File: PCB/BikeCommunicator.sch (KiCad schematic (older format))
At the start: 14 parts, among them SW1 SW_SPST_LED, SW2 SW_SPST_LED, SW3 SW_SPST_LED, SW4 SW_SPST_LED, U1 HW-108_DC-DC, U2 HTCC-AB01

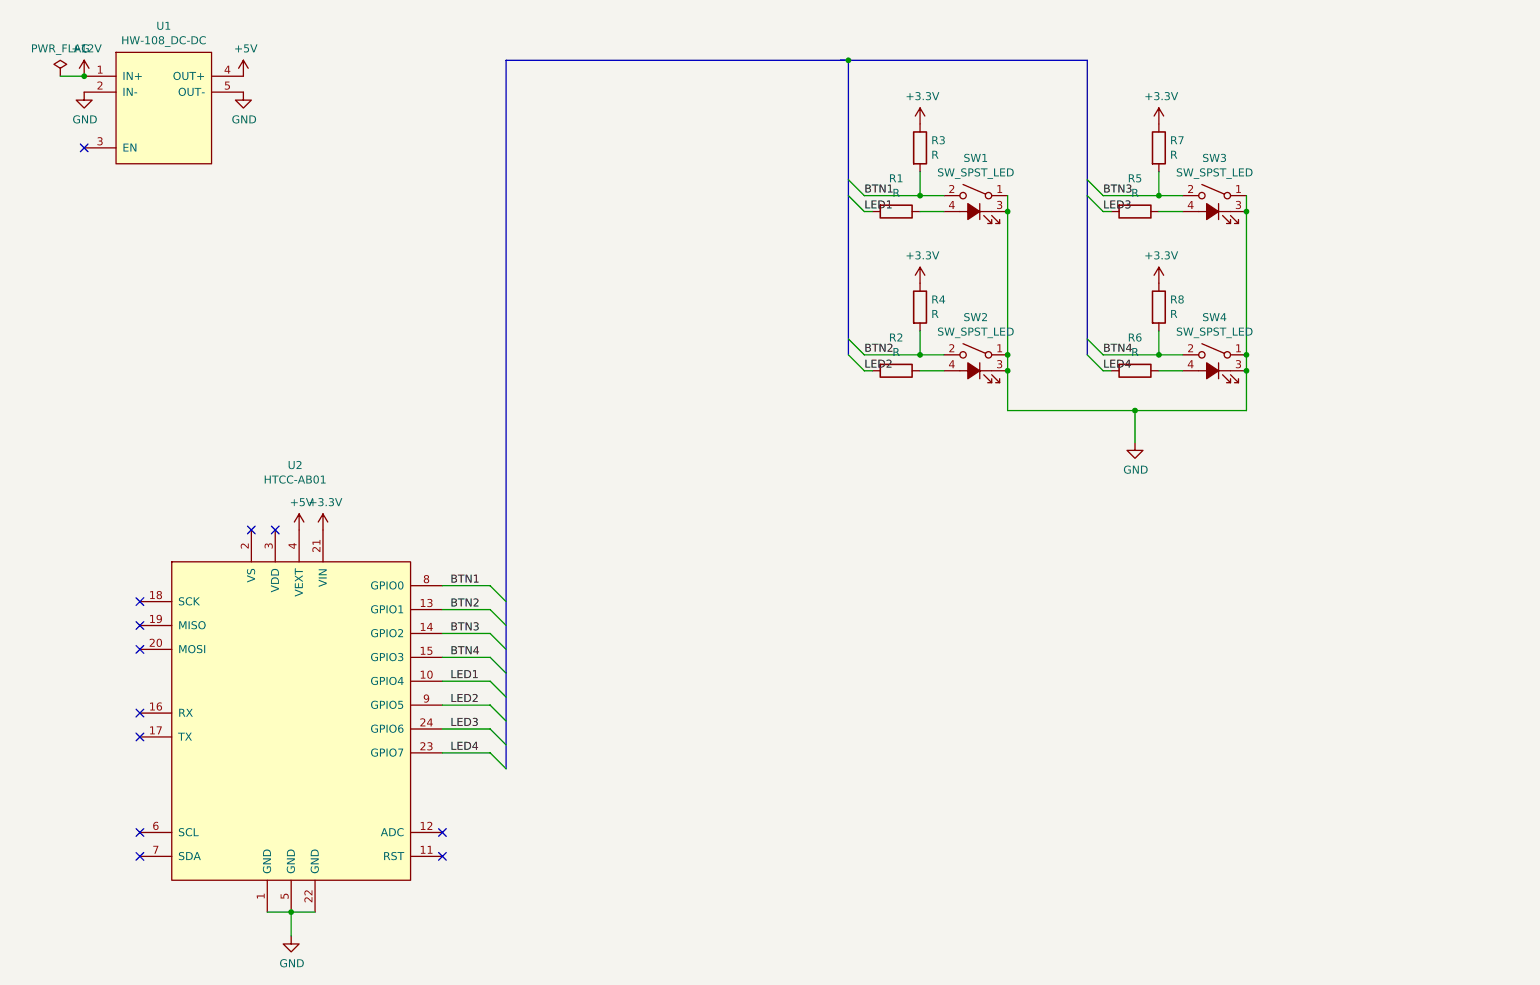
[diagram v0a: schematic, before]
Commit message: Fit PCB to housing, added some more elements to scheme
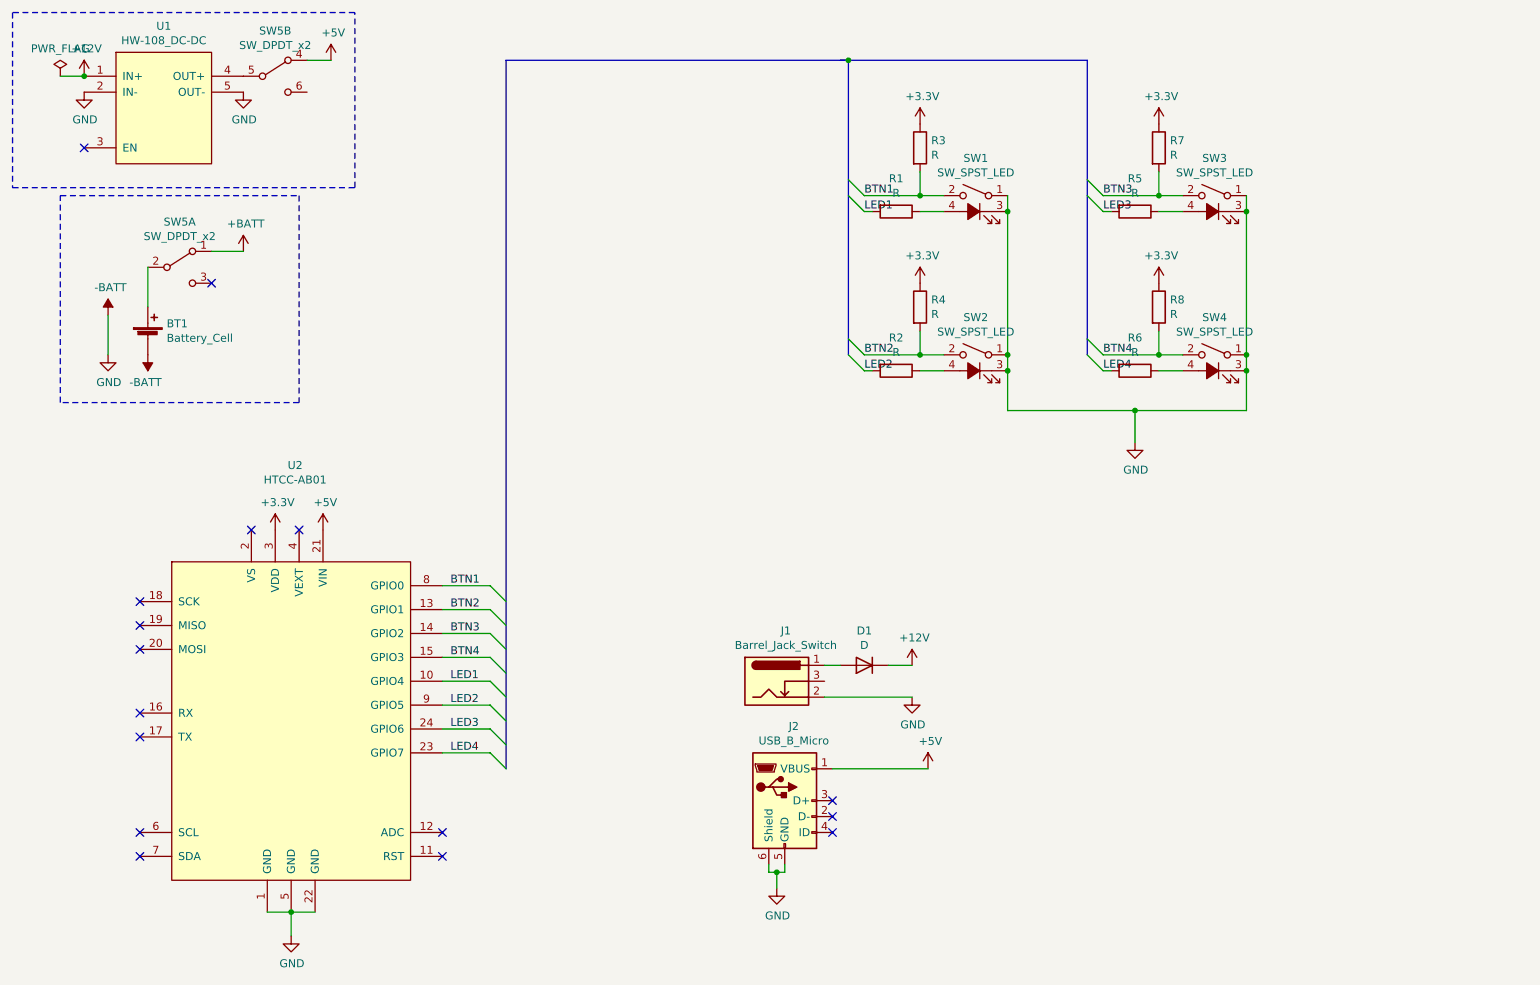
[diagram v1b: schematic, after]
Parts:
- added BT1: Battery_Cell, Connector_Wire:SolderWirePad_1x02_P7.62mm_Drill2mm, symbol Device:Battery_Cell
- added D1: D, Diodes_THT:D_A-405_P7.62mm_Horizontal, symbol Device:D
- added J1: Barrel_Jack_Switch, Connectors:BARREL_JACK, symbol Connector:Barrel_Jack_Switch
- added J2: USB_B_Micro, Connectors_USB:USB_Micro-B_Molex-105017-0001, symbol Connector:USB_B_Micro
- added SW5: SW_DPDT_x2, Buttons_Switches_THT:SW_CuK_JS202011AQN_DPDT_Angled, symbol Switch:SW_DPDT_x2
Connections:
- net +12V: now also D1.1 (K)
- net +3V3: now also U2.3 (VDD); no longer U2.21 (VIN)
- net +5V: now also U2.21 (VIN), J2.1 (VBUS), SW5.4 (A); no longer U1.4 (OUT+), U2.4 (VEXT)
- net GND renamed -BATT
- net -BATT: now also BT1.2 (-), J1.2, J2.5 (GND), J2.6 (Shield)
- new net: SW5.5 (B), U1.4 (OUT+)
- new net: BT1.1 (+), SW5.2 (B)
- new net: D1.2 (A), J1.1
- new net +BATT: SW5.1 (A)
- no-connect marks 12 -> 16
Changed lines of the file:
@@
 $EndComp
 NoConn ~ 2950 3750
-NoConn ~ 3100 3750
 Entry Wire Line
 	4450 5150 4550 5250
@@
 Text Label 4200 5150 0    50   ~ 0
 LED4
-Wire Bus Line
-	8200 800  8200 2650
-Wire Bus Line
-	6700 800  6700 2650
-Wire Bus Line
-	4550 800  4550 5250
 $Comp
 L MCU_Module:HTCC-AB01 U2
@@
 L power:+5V #PWR0101
 U 1 1 5EDD6E10
-P 3250 3750
-F 0 "#PWR0101" H 3250 3600 50  0001 C CNN
-F 1 "+5V" H 3265 3923 50  0000 C CNN
-F 2 "" H 3250 3750 50  0001 C CNN
-F 3 "" H 3250 3750 50  0001 C CNN
-	1    3250 3750
-	1    0    0    -1
-$EndComp
-$Comp
-L power:+5V #PWR0102
-U 1 1 5EDD979D
-P 2900 900
-F 0 "#PWR0102" H 2900 750 50  0001 C CNN
-F 1 "+5V" H 2915 1073 50  0000 C CNN
-F 2 "" H 2900 900 50  0001 C CNN
-F 3 "" H 2900 900 50  0001 C CNN
-	1    2900 900
-	1    0    0    -1
-$EndComp
-$Comp
-L power:+3.3V #PWR?
-U 1 1 5EDDB284
 P 3400 3750
-F 0 "#PWR?" H 3400 3600 50  0001 C CNN
-F 1 "+3.3V" H 3415 3923 50  0000 C CNN
+F 0 "#PWR0101" H 3400 3600 50  0001 C CNN
+F 1 "+5V" H 3415 3923 50  0000 C CNN
 F 2 "" H 3400 3750 50  0001 C CNN
 F 3 "" H 3400 3750 50  0001 C CNN
@@
 	1    0    0    -1
 $EndComp
+$Comp
+L power:+5V #PWR0102
+U 1 1 5EDD979D
+P 3450 800
+F 0 "#PWR0102" H 3450 650 50  0001 C CNN
+F 1 "+5V" H 3465 973 50  0000 C CNN
+F 2 "" H 3450 800 50  0001 C CNN
+F 3 "" H 3450 800 50  0001 C CNN
+	1    3450 800
+	1    0    0    -1
+$EndComp
+$Comp
+L Device:Battery_Cell BT1
+U 1 1 5EE175FB
+P 2300 2550
+F 0 "BT1" H 2418 2646 50  0000 L CNN
+F 1 "Battery_Cell" H 2418 2555 50  0000 L CNN
+F 2 "Connector_Wire:SolderWirePad_1x02_P7.62mm_Drill2mm" V 2300 2610 50  0001 C CNN
+F 3 "~" V 2300 2610 50  0001 C CNN
+	1    2300 2550
+	1    0    0    -1
+$EndComp
+$Comp
+L power:+BATT #PWR013
+U 1 1 5EE18CF7
+P 2900 2000
+F 0 "#PWR013" H 2900 1850 50  0001 C CNN
+F 1 "+BATT" H 2915 2173 50  0000 C CNN
+F 2 "" H 2900 2000 50  0001 C CNN
+F 3 "" H 2900 2000 50  0001 C CNN
+	1    2900 2000
+	1    0    0    -1
+$EndComp
+$Comp
+L power:GND #PWR06
+U 1 1 5EE196D1
+P 2050 2650
+F 0 "#PWR06" H 2050 2400 50  0001 C CNN
+F 1 "GND" H 2055 2477 50  0000 C CNN
+F 2 "" H 2050 2650 50  0001 C CNN
+F 3 "" H 2050 2650 50  0001 C CNN
+	1    2050 2650
+	1    0    0    -1
+$EndComp
+$Comp
+L power:-BATT #PWR03
+U 1 1 5EE19939
+P 2050 2400
+F 0 "#PWR03" H 2050 2250 50  0001 C CNN
+F 1 "-BATT" H 2065 2573 50  0000 C CNN
+F 2 "" H 2050 2400 50  0001 C CNN
+F 3 "" H 2050 2400 50  0001 C CNN
+	1    2050 2400
+	1    0    0    -1
+$EndComp
+$Comp
+L power:-BATT #PWR012
+U 1 1 5EE1A56E
+P 2300 2650
+F 0 "#PWR012" H 2300 2500 50  0001 C CNN
+F 1 "-BATT" H 2315 2823 50  0000 C CNN
+F 2 "" H 2300 2650 50  0001 C CNN
+F 3 "" H 2300 2650 50  0001 C CNN
+	1    2300 2650
+	-1   0    0    1
+$EndComp
+Wire Wire Line
+	2300 2350 2300 2100
+Wire Wire Line
+	2050 2400 2050 2650
+Wire Wire Line
+	2700 2000 2900 2000
+NoConn ~ 2700 2200
+$Comp
+L Switch:SW_DPDT_x2 SW5
+U 1 1 5EE2113C
+P 2500 2100
+F 0 "SW5" H 2500 2385 50  0000 C CNN
+F 1 "SW_DPDT_x2" H 2500 2294 50  0000 C CNN
+F 2 "Buttons_Switches_THT:SW_CuK_JS202011AQN_DPDT_Angled" H 2500 2100 50  0001 C CNN
+F 3 "~" H 2500 2100 50  0001 C CNN
+	1    2500 2100
+	1    0    0    -1
+$EndComp
+$Comp
+L Switch:SW_DPDT_x2 SW5
+U 2 1 5EE223ED
+P 3100 900
+F 0 "SW5" H 3100 1185 50  0000 C CNN
+F 1 "SW_DPDT_x2" H 3100 1094 50  0000 C CNN
+F 2 "Buttons_Switches_THT:SW_CuK_JS202011AQN_DPDT_Angled" H 3100 900 50  0001 C CNN
+F 3 "~" H 3100 900 50  0001 C CNN
+	2    3100 900
+	1    0    0    -1
+$EndComp
+Wire Wire Line
+	3300 800  3450 800
+Wire Notes Line
+	3250 1650 3250 2950
+Wire Notes Line
+	3250 2950 1750 2950
+Wire Notes Line
+	1750 2950 1750 1650
+Wire Notes Line
+	1750 1650 3250 1650
+Wire Notes Line
+	1450 500  1450 1600
+Wire Notes Line
+	1450 1600 3600 1600
+Wire Notes Line
+	3600 1600 3600 500
+Wire Notes Line
+	3600 500  1450 500
+$Comp
+L Connector:Barrel_Jack_Switch J1
+U 1 1 5EE445EB
+P 6250 4700
+F 0 "J1" H 6307 5017 50  0000 C CNN
+F 1 "Barrel_Jack_Switch" H 6307 4926 50  0000 C CNN
+F 2 "Connectors:BARREL_JACK" H 6300 4660 50  0001 C CNN
+F 3 "~" H 6300 4660 50  0001 C CNN
+	1    6250 4700
+	1    0    0    -1
+$EndComp
+$Comp
+L Connector:USB_B_Micro J2
+U 1 1 5EE4A85A
+P 6300 5450
+F 0 "J2" H 6357 5917 50  0000 C CNN
+F 1 "USB_B_Micro" H 6357 5826 50  0000 C CNN
+F 2 "Connectors_USB:USB_Micro-B_Molex-105017-0001" H 6450 5400 50  0001 C CNN
+F 3 "~" H 6450 5400 50  0001 C CNN
+	1    6300 5450
+	1    0    0    -1
+$EndComp
+NoConn ~ 6600 5450
+NoConn ~ 6600 5550
+NoConn ~ 6600 5650
+Wire Wire Line
+	6200 5850 6200 5900
+Wire Wire Line
+	6200 5900 6250 5900
+Wire Wire Line
+	6300 5900 6300 5850
+$Comp
+L power:GND #PWR015
+U 1 1 5EE4FB3E
+P 6250 6000
+F 0 "#PWR015" H 6250 5750 50  0001 C CNN
+F 1 "GND" H 6255 5827 50  0000 C CNN
+F 2 "" H 6250 6000 50  0001 C CNN
+F 3 "" H 6250 6000 50  0001 C CNN
+	1    6250 6000
+	1    0    0    -1
+$EndComp
+Wire Wire Line
+	6250 6000 6250 5900
+Connection ~ 6250 5900
+Wire Wire Line
+	6250 5900 6300 5900
+$Comp
+L power:+12V #PWR017
+U 1 1 5EE5C716
+P 7100 4600
+F 0 "#PWR017" H 7100 4450 50  0001 C CNN
+F 1 "+12V" H 7115 4773 50  0000 C CNN
+F 2 "" H 7100 4600 50  0001 C CNN
+F 3 "" H 7100 4600 50  0001 C CNN
+	1    7100 4600
+	1    0    0    -1
+$EndComp
+$Comp
+L power:+5V #PWR018
+U 1 1 5EE5CC8E
+P 7200 5250
+F 0 "#PWR018" H 7200 5100 50  0001 C CNN
+F 1 "+5V" H 7215 5423 50  0000 C CNN
+F 2 "" H 7200 5250 50  0001 C CNN
+F 3 "" H 7200 5250 50  0001 C CNN
+	1    7200 5250
+	1    0    0    -1
+$EndComp
+Wire Wire Line
+	6550 4600 6650 4600
+Wire Wire Line
+	6950 4600 7100 4600
+$Comp
+L power:GND #PWR016
+U 1 1 5EE65E7C
+P 7100 4800
+F 0 "#PWR016" H 7100 4550 50  0001 C CNN
+F 1 "GND" H 7105 4627 50  0000 C CNN
+F 2 "" H 7100 4800 50  0001 C CNN
+F 3 "" H 7100 4800 50  0001 C CNN
+	1    7100 4800
+	1    0    0    -1
+$EndComp
+Wire Wire Line
+	6600 5250 7200 5250
+NoConn ~ 3250 3750
+$Comp
+L power:+3.3V #PWR014
+U 1 1 5EE72401
+P 3100 3750
+F 0 "#PWR014" H 3100 3600 50  0001 C CNN
+F 1 "+3.3V" H 3115 3923 50  0000 C CNN
+F 2 "" H 3100 3750 50  0001 C CNN
+F 3 "" H 3100 3750 50  0001 C CNN
+	1    3100 3750
+	1    0    0    -1
+$EndComp
+$Comp
+L Device:D D1
+U 1 1 5EE8702B
+P 6800 4600
+F 0 "D1" H 6800 4383 50  0000 C CNN
+F 1 "D" H 6800 4474 50  0000 C CNN
+F 2 "Diodes_THT:D_A-405_P7.62mm_Horizontal" H 6800 4600 50  0001 C CNN
+F 3 "~" H 6800 4600 50  0001 C CNN
+	1    6800 4600
+	-1   0    0    1
+$EndComp
+Wire Wire Line
+	6550 4800 7100 4800
+Wire Bus Line
+	8200 800  8200 2650
+Wire Bus Line
+	6700 800  6700 2650
+Wire Bus Line
+	4550 800  4550 5250
 $EndSCHEMATC

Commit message: Redesigned PCB and housing to fit it.
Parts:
- added D2: D, Diodes_THT:D_A-405_P7.62mm_Horizontal, symbol Device:D
- added H1, H2, H3, H4: MountingHole_Pad, MountingHole:MountingHole_3.2mm_M3_Pad_Via, symbol Mechanical:MountingHole_Pad
- added J3: Conn_01x04, Connector_Wire:SolderWirePad_1x04_P3.81mm_Drill1mm, symbol Connector_Generic:Conn_01x04
- added J4: Conn_01x02, Connector_Wire:SolderWirePad_1x02_P3.81mm_Drill1mm, symbol Connector_Generic:Conn_01x02
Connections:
- net +5V: now also D2.1 (K), J3.1 (Pin_1); no longer J2.1 (VBUS)
- net +BATT: now also J4.2 (Pin_2)
- net -BATT: now also H1.1, H2.1, H3.1, H4.1, J3.4 (Pin_4), J4.1 (Pin_1)
- net USBD-: now reaches J2.2 (D-)
- net USBD-: now also J3.3 (Pin_3)
- net USBD+: now reaches J2.3 (D+)
- net USBD+: now also J3.2 (Pin_2)
- new net: D2.2 (A), J2.1 (VBUS)
- no-connect marks 16 -> 14
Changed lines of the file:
@@
 F 1 "HTCC-AB01" H 3225 6465 50  0000 C CNN
 F 2 "Modules:HTCC-AB01" H 2900 5350 50  0001 C CNN
-F 3 "" H 2900 5350 50  0001 C CNN
+F 3 "https://resource.heltec.cn/download/CubeCell/HTCC-AB01/HTCC-AB01_SchematicDiagram.pdf" H 2900 5350 50  0001 C CNN
 	1    3200 4950
 	1    0    0    -1
@@
 	1    0    0    -1
 $EndComp
-NoConn ~ 6600 5450
-NoConn ~ 6600 5550
 NoConn ~ 6600 5650
 Wire Wire Line
@@
 	1    0    0    -1
 $EndComp
-Wire Wire Line
-	6600 5250 7200 5250
 NoConn ~ 3250 3750
 $Comp
@@
 Wire Wire Line
 	6550 4800 7100 4800
+$Comp
+L Connector_Generic:Conn_01x04 J3
+U 1 1 5EE3CD6E
+P 7650 5450
+F 0 "J3" H 7730 5442 50  0000 L CNN
+F 1 "Conn_01x04" H 7730 5351 50  0000 L CNN
+F 2 "Connector_Wire:SolderWirePad_1x04_P3.81mm_Drill1mm" H 7650 5450 50  0001 C CNN
+F 3 "~" H 7650 5450 50  0001 C CNN
+	1    7650 5450
+	1    0    0    -1
+$EndComp
+Wire Wire Line
+	6300 5850 7450 5850
+Connection ~ 6300 5850
+Wire Wire Line
+	6600 5550 7450 5550
+Wire Wire Line
+	6600 5450 7450 5450
+Wire Wire Line
+	7450 5350 7200 5350
+Wire Wire Line
+	7200 5350 7200 5250
+Wire Wire Line
+	7450 5650 7450 5850
+Text Label 6600 5450 0    50   ~ 0
+USBD+
+Text Label 6600 5550 0    50   ~ 0
+USBD-
+$Comp
+L Connector_Generic:Conn_01x02 J4
+U 1 1 5EE50B8F
+P 3100 2400
+F 0 "J4" H 3018 2075 50  0000 C CNN
+F 1 "Conn_01x02" H 3018 2166 50  0000 C CNN
+F 2 "Connector_Wire:SolderWirePad_1x02_P3.81mm_Drill1mm" H 3100 2400 50  0001 C CNN
+F 3 "~" H 3100 2400 50  0001 C CNN
+	1    3100 2400
+	1    0    0    1
+$EndComp
+Wire Wire Line
+	2900 2000 2900 2300
+Connection ~ 2900 2000
+Wire Wire Line
+	2300 2650 2900 2650
+Wire Wire Line
+	2900 2650 2900 2400
+Connection ~ 2300 2650
+$Comp
+L Device:D D2
+U 1 1 5EE62A33
+P 6850 5250
+F 0 "D2" H 6850 5033 50  0000 C CNN
+F 1 "D" H 6850 5124 50  0000 C CNN
+F 2 "Diodes_THT:D_A-405_P7.62mm_Horizontal" H 6850 5250 50  0001 C CNN
+F 3 "~" H 6850 5250 50  0001 C CNN
+	1    6850 5250
+	-1   0    0    1
+$EndComp
+Wire Wire Line
+	6600 5250 6700 5250
+Wire Wire Line
+	7000 5250 7200 5250
+Connection ~ 7200 5250
+$Comp
+L Mechanical:MountingHole_Pad H1
+U 1 1 5EE693F5
+P 8900 4400
+F 0 "H1" H 9000 4449 50  0000 L CNN
+F 1 "MountingHole_Pad" H 9000 4358 50  0000 L CNN
+F 2 "MountingHole:MountingHole_3.2mm_M3_Pad_Via" H 8900 4400 50  0001 C CNN
+F 3 "~" H 8900 4400 50  0001 C CNN
+	1    8900 4400
+	1    0    0    -1
+$EndComp
+$Comp
+L Mechanical:MountingHole_Pad H2
+U 1 1 5EE69DE3
+P 9100 4400
+F 0 "H2" H 9200 4449 50  0000 L CNN
+F 1 "MountingHole_Pad" H 9200 4358 50  0000 L CNN
+F 2 "MountingHole:MountingHole_3.2mm_M3_Pad_Via" H 9100 4400 50  0001 C CNN
+F 3 "~" H 9100 4400 50  0001 C CNN
+	1    9100 4400
+	1    0    0    -1
+$EndComp
+$Comp
+L Mechanical:MountingHole_Pad H3
+U 1 1 5EE6A022
+P 9300 4400
+F 0 "H3" H 9400 4449 50  0000 L CNN
+F 1 "MountingHole_Pad" H 9400 4358 50  0000 L CNN
+F 2 "MountingHole:MountingHole_3.2mm_M3_Pad_Via" H 9300 4400 50  0001 C CNN
+F 3 "~" H 9300 4400 50  0001 C CNN
+	1    9300 4400
+	1    0    0    -1
+$EndComp
+$Comp
+L Mechanical:MountingHole_Pad H4
+U 1 1 5EE6A268
+P 9500 4400
+F 0 "H4" H 9600 4449 50  0000 L CNN
+F 1 "MountingHole_Pad" H 9600 4358 50  0000 L CNN
+F 2 "MountingHole:MountingHole_3.2mm_M3_Pad_Via" H 9500 4400 50  0001 C CNN
+F 3 "~" H 9500 4400 50  0001 C CNN
+	1    9500 4400
+	1    0    0    -1
+$EndComp
+Wire Wire Line
+	8900 4500 9100 4500
+Wire Wire Line
+	9100 4500 9300 4500
+Connection ~ 9100 4500
+Wire Wire Line
+	9300 4500 9500 4500
 Wire Bus Line
 	8200 800  8200 2650
@@
 Wire Bus Line
 	4550 800  4550 5250
+Connection ~ 9300 4500
+$Comp
+L power:GND #PWR019
+U 1 1 5EE6F33F
+P 8900 4500
+F 0 "#PWR019" H 8900 4250 50  0001 C CNN
+F 1 "GND" H 8905 4327 50  0000 C CNN
+F 2 "" H 8900 4500 50  0001 C CNN
+F 3 "" H 8900 4500 50  0001 C CNN
+	1    8900 4500
+	1    0    0    -1
+$EndComp
+Connection ~ 8900 4500
 $EndSCHEMATC
